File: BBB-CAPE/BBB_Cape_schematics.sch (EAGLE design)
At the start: 84 parts, among them IC1 EEPROM-I2CSMD, SW2 219-02

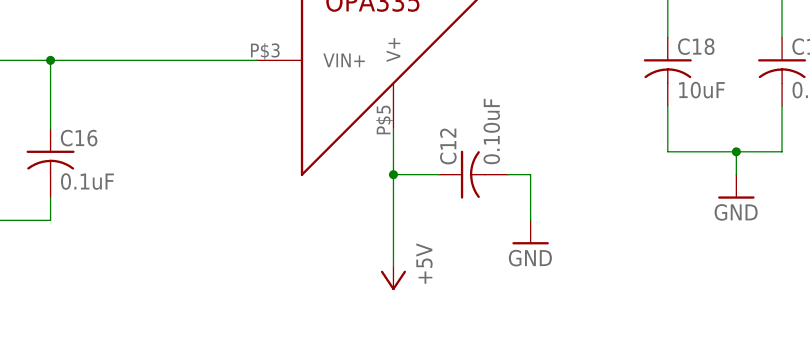
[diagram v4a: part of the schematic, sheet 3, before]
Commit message: Place components and Route for -5V, 2.5V supply in BBB_Cape_schematics.brd and Change +5V to 5V in BBB_schematics.sch
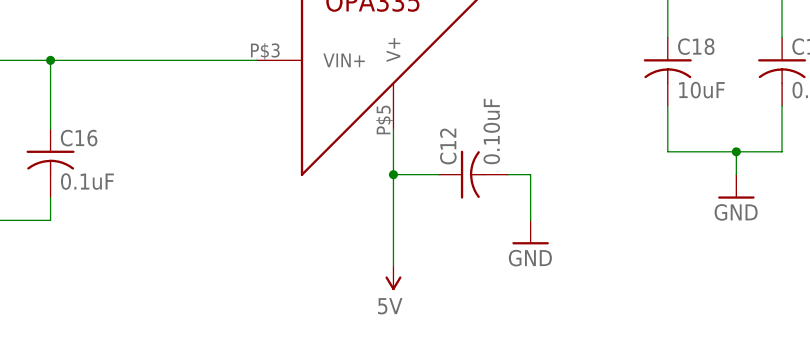
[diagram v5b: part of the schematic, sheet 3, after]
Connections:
- net +5V: no longer C12.1, U$22.V+
- net 5V: now also C12.1, U$22.V+
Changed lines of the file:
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@@
 <part name="GND28" library="supply1" deviceset="GND" device=""/>
 <part name="JP5" library="jumper" deviceset="JP2E" device=""/>
-<part name="P+14" library="supply1" deviceset="+5V" device=""/>
 <part name="C12" library="rcl" deviceset="C-US" device="C1206" value="0.10uF"/>
 <part name="GND30" library="supply1" deviceset="GND" device=""/>
@@
 <part name="C22" library="rcl" deviceset="C-US" device="C1206" value="22pF"/>
 <part name="U$26" library="SparkFun-Aesthetics" deviceset="5V" device=""/>
+<part name="U$27" library="SparkFun-Aesthetics" deviceset="5V" device=""/>
 </parts>
 <sheets>
@@
 </instance>
 <instance part="P+13" gate="G$1" x="248.92" y="203.2"/>
-<instance part="P+14" gate="1" x="162.56" y="50.8" rot="R180"/>
 <instance part="C12" gate="G$1" x="170.18" y="63.5" rot="R90"/>
 <instance part="GND30" gate="1" x="177.8" y="55.88"/>
 <instance part="U$26" gate="G$1" x="53.34" y="86.36"/>
+<instance part="U$27" gate="G$1" x="162.56" y="53.34" rot="R180"/>
 </instances>
 <busses>
@@
 <junction x="53.34" y="76.2"/>
 </segment>
-</net>
-<net name="+5V" class="0">
 <segment>
 <pinref part="U$22" gate="G$1" pin="V+"/>
-<pinref part="P+14" gate="1" pin="+5V"/>
 <wire x1="162.56" y1="68.58" x2="162.56" y2="63.5" width="0.1524" layer="91"/>
 <pinref part="C12" gate="G$1" pin="1"/>
@@
 <wire x1="167.64" y1="63.5" x2="162.56" y2="63.5" width="0.1524" layer="91"/>
 <junction x="162.56" y="63.5"/>
-</segment>
-</net>
+<pinref part="U$27" gate="G$1" pin="5V"/>
+</segment>
+</net>

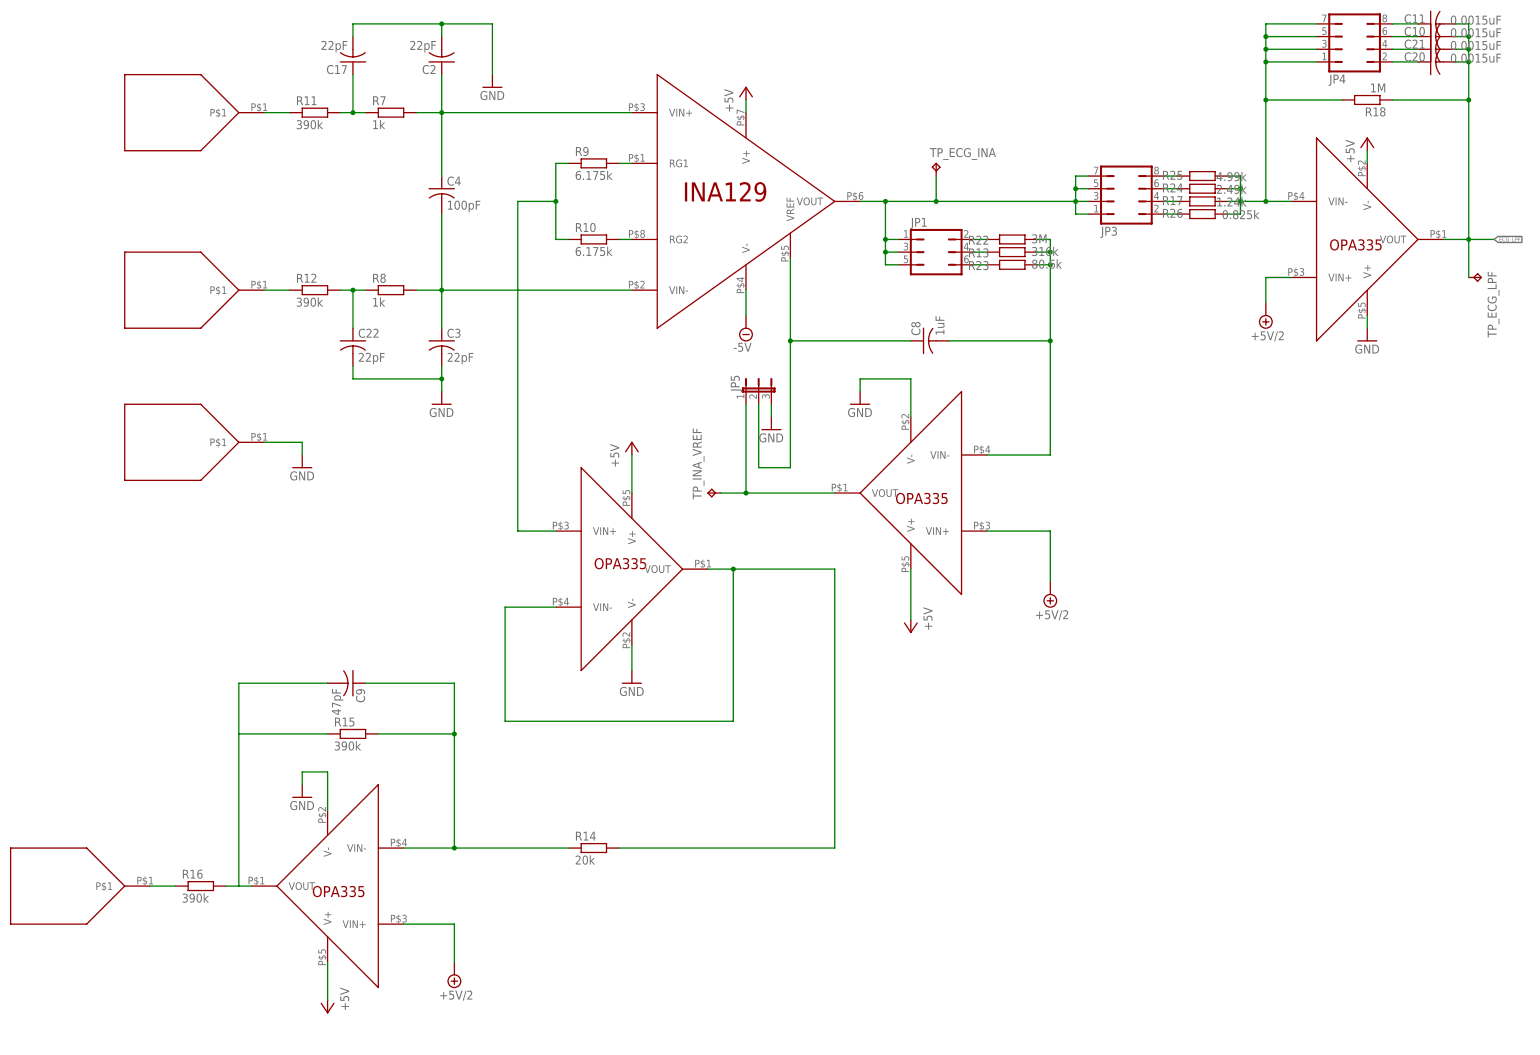
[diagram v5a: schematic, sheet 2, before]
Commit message: Solved error caused by imporper node connection across C4 and removed ERC errors in BBB_Cape_schematics.sch
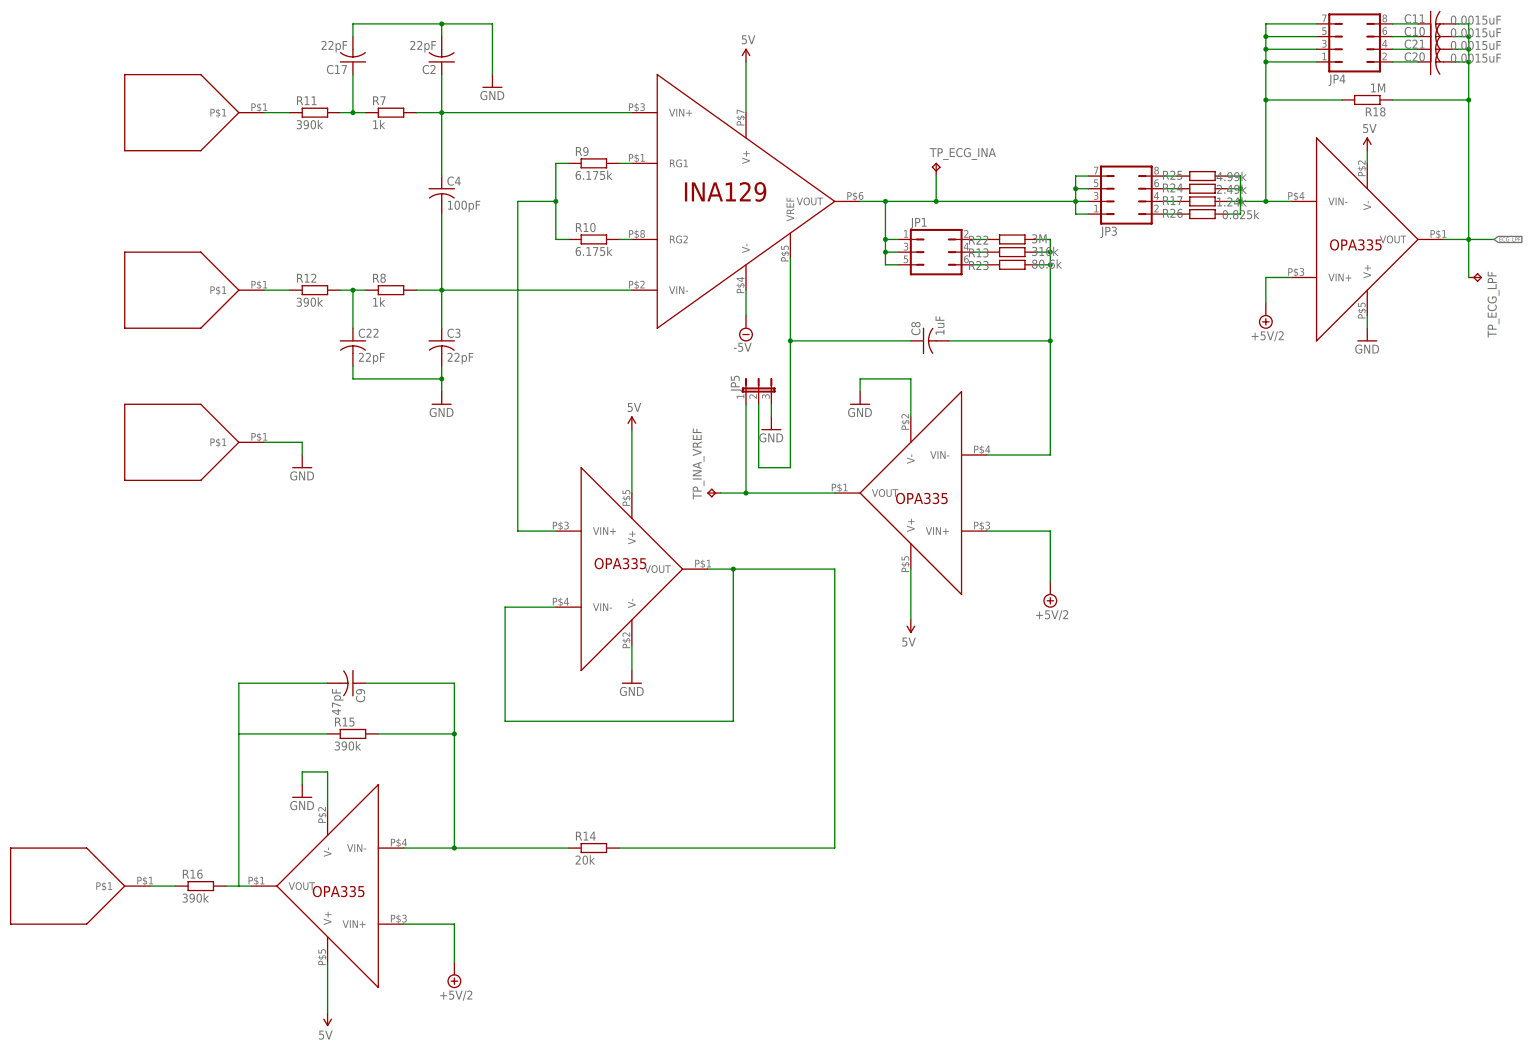
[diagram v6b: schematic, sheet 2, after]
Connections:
- removed net +5V: U$11.V+, U$12.V+, U$13.V-, U$4.V+, U$9.V+
- new net N$20: C2.1
- new net N$36: C3.1
- net 5V: now also U$11.V+, U$12.V+, U$13.V-, U$4.V+, U$9.V+
- net N$1: no longer C2.1
- net N$2: no longer C3.1
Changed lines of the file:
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@@
 <setting verticaltext="up"/>
 </settings>
-<grid distance="0.1" unitdist="inch" unit="inch" style="lines" multiple="1" display="no" altdistance="0.01" altunitdist="inch" altunit="inch"/>
+<grid distance="0.1" unitdist="inch" unit="inch" style="lines" multiple="1" display="yes" altdistance="0.01" altunitdist="inch" altunit="inch"/>
 <layers>
 <layer number="1" name="Top" color="4" fill="1" visible="no" active="no"/>
@@
 <part name="U$7" library="SparkFun-Aesthetics" deviceset="5V" device=""/>
 <part name="SUPPLY1" library="supply2" deviceset="-5V" device=""/>
-<part name="P+3" library="supply1" deviceset="+5V" device=""/>
 <part name="SUPPLY2" library="supply2" deviceset="-5V" device=""/>
-<part name="P+4" library="supply1" deviceset="+5V" device=""/>
 <part name="C8" library="rcl" deviceset="C-US" device="C1206" value="1uF"/>
 <part name="R13" library="resistor" deviceset="R-EU_" device="M1206" value="316k"/>
 <part name="U$9" library="Components" deviceset="OPA335" device=""/>
 <part name="U$11" library="Components" deviceset="OPA335" device=""/>
-<part name="P+5" library="supply1" deviceset="+5V" device=""/>
 <part name="GND13" library="supply1" deviceset="GND" device=""/>
 <part name="GND15" library="supply1" deviceset="GND" device=""/>
@@
 <part name="C9" library="rcl" deviceset="C-US" device="C1206" value="47pF"/>
 <part name="GND16" library="supply1" deviceset="GND" device=""/>
-<part name="P+8" library="supply1" deviceset="+5V" device=""/>
 <part name="SUPPLY4" library="supply2" deviceset="+5V/2" device=""/>
 <part name="SUPPLY5" library="supply2" deviceset="+5V/2" device=""/>
@@
 <part name="R18" library="resistor" deviceset="R-EU_" device="M1206" value="1M"/>
 <part name="SUPPLY6" library="supply2" deviceset="+5V/2" device=""/>
-<part name="P+10" library="supply1" deviceset="+5V" device=""/>
 <part name="GND19" library="supply1" deviceset="GND" device=""/>
 <part name="U$14" library="Components" deviceset="OPA335" device=""/>
@@
 <part name="U$26" library="SparkFun-Aesthetics" deviceset="5V" device=""/>
 <part name="U$27" library="SparkFun-Aesthetics" deviceset="5V" device=""/>
+<part name="U$28" library="SparkFun-Aesthetics" deviceset="5V" device=""/>
+<part name="U$29" library="SparkFun-Aesthetics" deviceset="5V" device=""/>
+<part name="U$30" library="SparkFun-Aesthetics" deviceset="5V" device=""/>
+<part name="U$31" library="SparkFun-Aesthetics" deviceset="5V" device=""/>
+<part name="U$32" library="SparkFun-Aesthetics" deviceset="5V" device=""/>
 </parts>
 <sheets>
@@
 </instance>
 <instance part="R12" gate="G$1" x="96.52" y="170.18"/>
-<instance part="P+3" gate="1" x="182.88" y="210.82"/>
 <instance part="SUPPLY2" gate="-5V" x="182.88" y="162.56"/>
-<instance part="P+4" gate="1" x="215.9" y="101.6" rot="R180"/>
 <instance part="C8" gate="G$1" x="218.44" y="160.02" rot="R90"/>
 <instance part="R13" gate="G$1" x="236.22" y="177.8" smashed="yes">
@@
 <instance part="U$9" gate="G$1" x="215.9" y="129.54" rot="R180"/>
 <instance part="U$11" gate="G$1" x="160.02" y="114.3"/>
-<instance part="P+5" gate="1" x="160.02" y="139.7"/>
 <instance part="GND13" gate="1" x="160.02" y="91.44"/>
 <instance part="GND15" gate="1" x="205.74" y="147.32"/>
@@
 <instance part="C9" gate="G$1" x="104.14" y="91.44" rot="R270"/>
 <instance part="GND16" gate="1" x="93.98" y="68.58"/>
-<instance part="P+8" gate="1" x="99.06" y="25.4" rot="R180"/>
 <instance part="SUPPLY4" gate="G$1" x="124.46" y="33.02" rot="R180"/>
 <instance part="SUPPLY5" gate="G$1" x="243.84" y="109.22" rot="R180"/>
@@
 <instance part="R18" gate="G$1" x="307.34" y="208.28" rot="R180"/>
 <instance part="SUPPLY6" gate="G$1" x="287.02" y="165.1" rot="R180"/>
-<instance part="P+10" gate="1" x="307.34" y="200.66"/>
 <instance part="GND19" gate="1" x="307.34" y="160.02"/>
 <instance part="U$17" gate="G$1" x="68.58" y="205.74"/>
@@
 <instance part="C17" gate="G$1" x="104.14" y="215.9" rot="R180"/>
 <instance part="C22" gate="G$1" x="104.14" y="160.02"/>
+<instance part="U$28" gate="G$1" x="99.06" y="25.4" rot="R180"/>
+<instance part="U$29" gate="G$1" x="160.02" y="142.24"/>
+<instance part="U$30" gate="G$1" x="215.9" y="104.14" rot="R180"/>
+<instance part="U$31" gate="G$1" x="182.88" y="215.9"/>
+<instance part="U$32" gate="G$1" x="307.34" y="198.12"/>
 </instances>
 <busses>
@@
 <wire x1="121.92" y1="193.04" x2="121.92" y2="205.74" width="0.1524" layer="91"/>
 <junction x="121.92" y="205.74"/>
-<pinref part="C2" gate="G$1" pin="1"/>
-<wire x1="121.92" y1="213.36" x2="121.92" y2="205.74" width="0.1524" layer="91"/>
 </segment>
 </net>
@@
 <wire x1="121.92" y1="185.42" x2="121.92" y2="170.18" width="0.1524" layer="91"/>
 <junction x="121.92" y="170.18"/>
-<pinref part="C3" gate="G$1" pin="1"/>
-<wire x1="121.92" y1="162.56" x2="121.92" y2="170.18" width="0.1524" layer="91"/>
 </segment>
 </net>
@@
 <pinref part="SUPPLY2" gate="-5V" pin="-5V"/>
 <wire x1="182.88" y1="170.18" x2="182.88" y2="165.1" width="0.1524" layer="91"/>
-</segment>
-</net>
-<net name="+5V" class="0">
-<segment>
-<pinref part="P+3" gate="1" pin="+5V"/>
-<pinref part="U$4" gate="G$1" pin="V+"/>
-<wire x1="182.88" y1="208.28" x2="182.88" y2="205.74" width="0.1524" layer="91"/>
-</segment>
-<segment>
-<pinref part="P+4" gate="1" pin="+5V"/>
-<wire x1="215.9" y1="104.14" x2="215.9" y2="114.3" width="0.1524" layer="91"/>
-<pinref part="U$9" gate="G$1" pin="V+"/>
-</segment>
-<segment>
-<pinref part="P+5" gate="1" pin="+5V"/>
-<pinref part="U$11" gate="G$1" pin="V+"/>
-<wire x1="160.02" y1="137.16" x2="160.02" y2="129.54" width="0.1524" layer="91"/>
-</segment>
-<segment>
-<pinref part="P+8" gate="1" pin="+5V"/>
-<pinref part="U$12" gate="G$1" pin="V+"/>
-<wire x1="99.06" y1="27.94" x2="99.06" y2="35.56" width="0.1524" layer="91"/>
-</segment>
-<segment>
-<pinref part="P+10" gate="1" pin="+5V"/>
-<pinref part="U$13" gate="G$1" pin="V-"/>
-<wire x1="307.34" y1="198.12" x2="307.34" y2="195.58" width="0.1524" layer="91"/>
 </segment>
 </net>
@@
 </segment>
 </net>
+<net name="5V" class="0">
+<segment>
+<pinref part="U$28" gate="G$1" pin="5V"/>
+<pinref part="U$12" gate="G$1" pin="V+"/>
+<wire x1="99.06" y1="25.4" x2="99.06" y2="35.56" width="0.1524" layer="91"/>
+</segment>
+<segment>
+<pinref part="U$29" gate="G$1" pin="5V"/>
+<pinref part="U$11" gate="G$1" pin="V+"/>
+<wire x1="160.02" y1="142.24" x2="160.02" y2="129.54" width="0.1524" layer="91"/>
+</segment>
+<segment>
+<pinref part="U$31" gate="G$1" pin="5V"/>
+<pinref part="U$4" gate="G$1" pin="V+"/>
+<wire x1="182.88" y1="215.9" x2="182.88" y2="205.74" width="0.1524" layer="91"/>
+</segment>
+<segment>
+<pinref part="U$9" gate="G$1" pin="V+"/>
+<pinref part="U$30" gate="G$1" pin="5V"/>
+<wire x1="215.9" y1="114.3" x2="215.9" y2="104.14" width="0.1524" layer="91"/>
+</segment>
+<segment>
+<pinref part="U$13" gate="G$1" pin="V-"/>
+<pinref part="U$32" gate="G$1" pin="5V"/>
+<wire x1="307.34" y1="195.58" x2="307.34" y2="198.12" width="0.1524" layer="91"/>
+</segment>
+</net>
+<net name="N$20" class="0">
+<segment>
+<pinref part="C2" gate="G$1" pin="1"/>
+<wire x1="121.92" y1="213.36" x2="121.92" y2="205.74" width="0.1524" layer="91"/>
+</segment>
+</net>
+<net name="N$36" class="0">
+<segment>
+<pinref part="C3" gate="G$1" pin="1"/>
+<wire x1="121.92" y1="162.56" x2="121.92" y2="170.18" width="0.1524" layer="91"/>
+</segment>
+</net>

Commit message: Connect N$1 with N$20 and N$2 with N$36 in BBB_Cape_schematics.sch
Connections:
- removed net N$20: C2.1
- removed net N$36: C3.1
- net N$1: now also C2.1
- net N$2: now also C3.1
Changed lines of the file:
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@@
 <setting verticaltext="up"/>
 </settings>
-<grid distance="0.1" unitdist="inch" unit="inch" style="lines" multiple="1" display="yes" altdistance="0.01" altunitdist="inch" altunit="inch"/>
+<grid distance="0.1" unitdist="inch" unit="inch" style="lines" multiple="1" display="no" altdistance="0.01" altunitdist="inch" altunit="inch"/>
 <layers>
 <layer number="1" name="Top" color="4" fill="1" visible="no" active="no"/>
@@
 <junction x="121.92" y="205.74"/>
 </segment>
+<segment>
+<pinref part="C2" gate="G$1" pin="1"/>
+<wire x1="121.92" y1="213.36" x2="121.92" y2="205.74" width="0.1524" layer="91"/>
+</segment>
 </net>
 <net name="N$2" class="0">
@@
 <wire x1="121.92" y1="185.42" x2="121.92" y2="170.18" width="0.1524" layer="91"/>
 <junction x="121.92" y="170.18"/>
+</segment>
+<segment>
+<pinref part="C3" gate="G$1" pin="1"/>
+<wire x1="121.92" y1="162.56" x2="121.92" y2="170.18" width="0.1524" layer="91"/>
 </segment>
 </net>
@@
 </segment>
 </net>
-<net name="N$20" class="0">
-<segment>
-<pinref part="C2" gate="G$1" pin="1"/>
-<wire x1="121.92" y1="213.36" x2="121.92" y2="205.74" width="0.1524" layer="91"/>
-</segment>
-</net>
-<net name="N$36" class="0">
-<segment>
-<pinref part="C3" gate="G$1" pin="1"/>
-<wire x1="121.92" y1="162.56" x2="121.92" y2="170.18" width="0.1524" layer="91"/>
-</segment>
-</net>

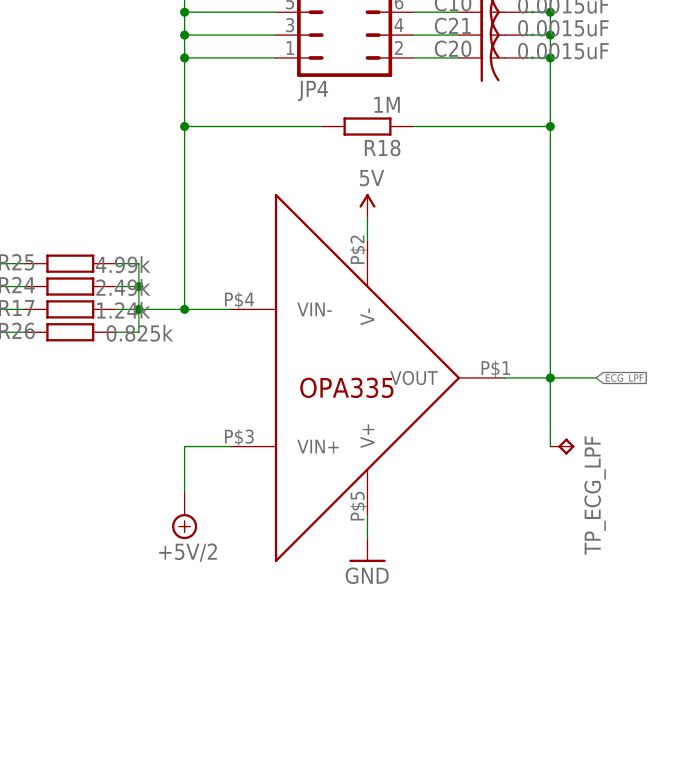
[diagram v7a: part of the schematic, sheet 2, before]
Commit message: Correct pin connection of U$13 Op-Amp in BBB_Cape_schematics.sch
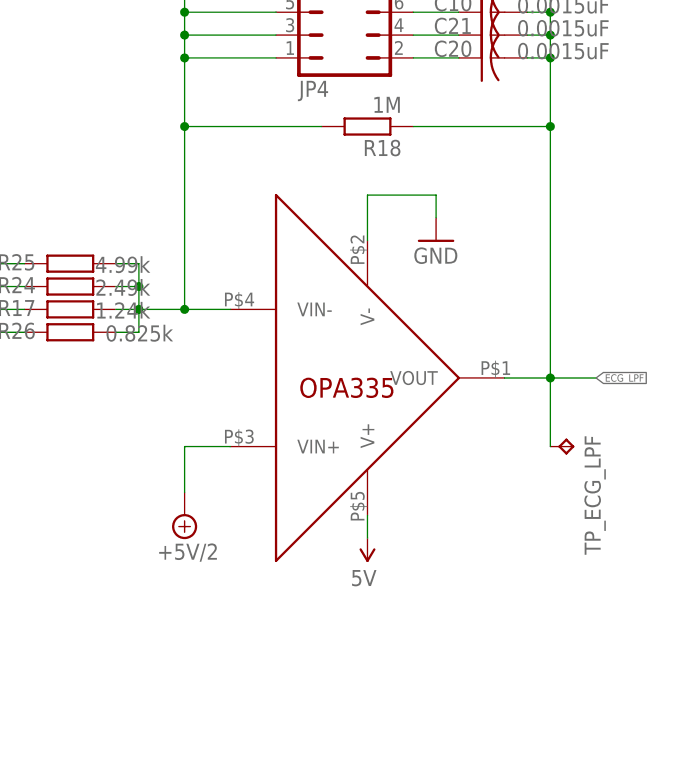
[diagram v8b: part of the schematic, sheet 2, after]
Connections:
- net 5V: now also U$13.V+; no longer U$13.V-
- net GND: now also U$13.V-; no longer U$13.V+
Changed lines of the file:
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@@
 <instance part="R18" gate="G$1" x="307.34" y="208.28" rot="R180"/>
 <instance part="SUPPLY6" gate="G$1" x="287.02" y="165.1" rot="R180"/>
-<instance part="GND19" gate="1" x="307.34" y="160.02"/>
+<instance part="GND19" gate="1" x="314.96" y="195.58"/>
 <instance part="U$17" gate="G$1" x="68.58" y="205.74"/>
 <instance part="U$16" gate="G$1" x="68.58" y="170.18"/>
@@
 <instance part="U$30" gate="G$1" x="215.9" y="104.14" rot="R180"/>
 <instance part="U$31" gate="G$1" x="182.88" y="215.9"/>
-<instance part="U$32" gate="G$1" x="307.34" y="198.12"/>
+<instance part="U$32" gate="G$1" x="307.34" y="162.56" rot="R180"/>
 </instances>
 <busses>
@@
 </segment>
 <segment>
-<pinref part="U$13" gate="G$1" pin="V+"/>
-<pinref part="GND19" gate="1" pin="GND"/>
-<wire x1="307.34" y1="165.1" x2="307.34" y2="162.56" width="0.1524" layer="91"/>
-</segment>
-<segment>
 <pinref part="U$24" gate="G$1" pin="P$1"/>
 <wire x1="86.36" y1="139.7" x2="93.98" y2="139.7" width="0.1524" layer="91"/>
@@
 <wire x1="104.14" y1="152.4" x2="121.92" y2="152.4" width="0.1524" layer="91"/>
 <junction x="121.92" y="152.4"/>
+</segment>
+<segment>
+<pinref part="U$13" gate="G$1" pin="V-"/>
+<wire x1="307.34" y1="195.58" x2="307.34" y2="200.66" width="0.1524" layer="91"/>
+<pinref part="GND19" gate="1" pin="GND"/>
+<wire x1="307.34" y1="200.66" x2="314.96" y2="200.66" width="0.1524" layer="91"/>
+<wire x1="314.96" y1="200.66" x2="314.96" y2="198.12" width="0.1524" layer="91"/>
 </segment>
 </net>
@@
 </segment>
 <segment>
-<pinref part="U$13" gate="G$1" pin="V-"/>
+<pinref part="U$13" gate="G$1" pin="V+"/>
 <pinref part="U$32" gate="G$1" pin="5V"/>
-<wire x1="307.34" y1="195.58" x2="307.34" y2="198.12" width="0.1524" layer="91"/>
-</segment>
-</net>
+<wire x1="307.34" y1="165.1" x2="307.34" y2="162.56" width="0.1524" layer="91"/>
+</segment>
+</net>
